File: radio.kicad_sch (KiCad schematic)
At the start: 27 parts, among them IC4 S2-LPQTR, IC5 BALF-SPI2-01D3, Y3 Crystal_GND24

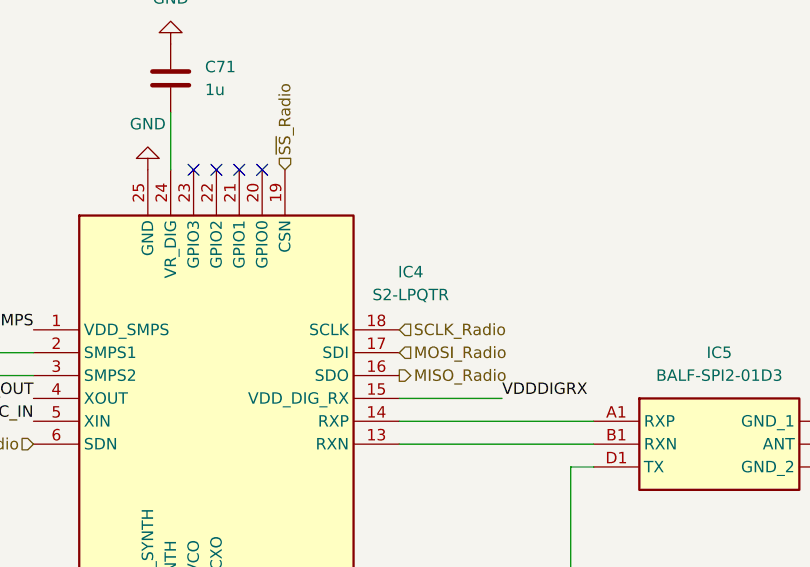
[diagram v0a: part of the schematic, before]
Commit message: Modify symbols of LDO and S2LP
Symbols for LDO and S2LP are inconsistent, because LDO VOUT pin was not in POWER OUTPUT type and S2LP wait for POWER INPUT on VDDS ... Moreover, decoupling capacitors on S2LP was a hell, because ERC break power flag transitivity on all passive components
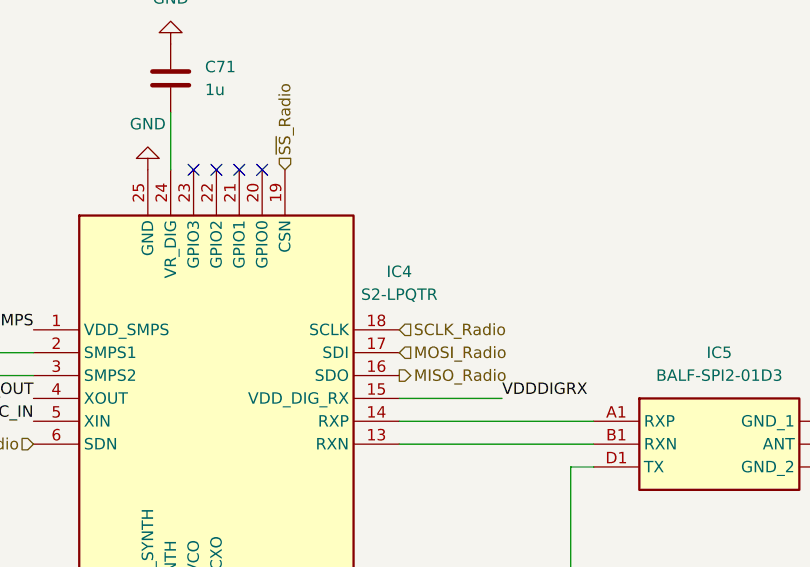
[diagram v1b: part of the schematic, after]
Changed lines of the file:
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@@
+	)
+	(symbol
+		(lib_id "weather-station-poc-sym:S2-LPQTR")
+		(at 127 74.93 0)
+		(unit 1)
+		(exclude_from_sim no)
+		(in_bom yes)
+		(on_board yes)
+		(dnp no)
+		(fields_autoplaced yes)
+		(property "Reference" "IC4"
+			(at 167.64 68.4745 0)
+			(effects
+				(font
+					(size 1.27 1.27)
+				)
+			)
+		)
+		(property "Value" "S2-LPQTR"
+			(at 167.64 71.0145 0)
+			(effects
+				(font
+					(size 1.27 1.27)
+				)
+			)
+		)
+		(property "Footprint" "weather-station-poc-fp:QFN50P400X400X100-25N-D"
+			(at 163.83 159.69 0)
+			(effects
+				(font
+					(size 1.27 1.27)
+				)
+				(justify left top)
+				(hide yes)
+			)
+		)
+		(property "Datasheet" "http://www.st.com/content/ccc/resource/technical/document/datasheet/group3/bd/26/62/81/3d/86/4d/15/DM00339133/files/DM00339133.pdf/jcr:content/translations/en.DM00339133.pdf"
+			(at 163.83 259.69 0)
+			(effects
+				(font
+					(size 1.27 1.27)
+				)
+				(justify left top)
+				(hide yes)
+			)
+		)
+		(property "Description" "STMICROELECTRONICS - S2-LPQTR - RF TRANSCEIVER, 1GHZ, QFN-24"
+			(at 127 74.93 0)
+			(effects
+				(font
+					(size 1.27 1.27)
+				)
+				(hide yes)
+			)
+		)
+		(property "Height" "1"
+			(at 163.83 459.69 0)
+			(effects
+				(font
+					(size 1.27 1.27)
+				)
+				(justify left top)
+				(hide yes)
+			)
+		)
+		(property "Mouser Part Number" "511-S2-LPQTR"
+			(at 163.83 559.69 0)
+			(effects
+				(font
+					(size 1.27 1.27)
+				)
+				(justify left top)
+				(hide yes)
+			)
+		)
+		(property "Mouser Price/Stock" "https://www.mouser.co.uk/ProductDetail/STMicroelectronics/S2-LPQTR?qs=pBOFM1sAujt3j15q4uNAuQ%3D%3D"
+			(at 163.83 659.69 0)
+			(effects
+				(font
+					(size 1.27 1.27)
+				)
+				(justify left top)
+				(hide yes)
+			)
+		)
+		(property "Manufacturer_Name" "STMicroelectronics"
+			(at 163.83 759.69 0)
+			(effects
+				(font
+					(size 1.27 1.27)
+				)
+				(justify left top)
+				(hide yes)
+			)
+		)
+		(property "Manufacturer_Part_Number" "S2-LPQTR"
+			(at 163.83 859.69 0)
+			(effects
+				(font
+					(size 1.27 1.27)
+				)
+				(justify left top)
+				(hide yes)
+			)
+		)
+		(pin "24"
+		)
+		(pin "12"
+		)
+		(pin "14"
+		)
+		(pin "20"
+		)
+		(pin "23"
+		)
+		(pin "8"
+		)
+		(pin "22"
+		)
+		(pin "17"
+		)
+		(pin "19"
+		)
+		(pin "6"
+		)
+		(pin "25"
+		)
+		(pin "21"
+		)
+		(pin "3"
+		)
+		(pin "10"
+		)
+		(pin "18"
+		)
+		(pin "2"
+		)
+		(pin "4"
+		)
+		(pin "9"
+		)
+		(pin "13"
+		)
+		(pin "11"
+		)
+		(pin "16"
+		)
+		(pin "1"
+		)
+		(pin "7"
+		)
+		(pin "15"
+		)
+		(pin "5"
+		)
+		(instances
+			(project ""
+				(path "/38eb53bb-294e-46e4-ad59-fd355ca373b9/31741ecc-719f-4191-b75e-d75152dfd251"
+					(reference "IC4")
+					(unit 1)
+				)
+			)
+		)
 	)
 	(symbol
@@
 					(unit 1)
 				)
-			)
-		)
-	)
-	(symbol
-		(lib_id "weather-station-poc-sym:S2-LPQTR")
-		(at 127 74.93 0)
-		(unit 1)
-		(exclude_from_sim no)
-		(in_bom yes)
-		(on_board yes)
-		(dnp no)
-		(fields_autoplaced yes)
-		(property "Reference" "IC4"
-			(at 168.91 68.5098 0)
-			(effects
-				(font
-					(size 1.27 1.27)
-				)
-			)
-		)
-		(property "Value" "S2-LPQTR"
-			(at 168.91 71.0498 0)
-			(effects
-				(font
-					(size 1.27 1.27)
-				)
-			)
-		)
-		(property "Footprint" "weather-station-poc-fp:QFN50P400X400X100-25N-D"
-			(at 163.83 159.69 0)
-			(effects
-				(font
-					(size 1.27 1.27)
-				)
-				(justify left top)
-				(hide yes)
-			)
-		)
-		(property "Datasheet" "http://www.st.com/content/ccc/resource/technical/document/datasheet/group3/bd/26/62/81/3d/86/4d/15/DM00339133/files/DM00339133.pdf/jcr:content/translations/en.DM00339133.pdf"
-			(at 163.83 259.69 0)
-			(effects
-				(font
-					(size 1.27 1.27)
-				)
-				(justify left top)
-				(hide yes)
-			)
-		)
-		(property "Description" "STMICROELECTRONICS - S2-LPQTR - RF TRANSCEIVER, 1GHZ, QFN-24"
-			(at 127 74.93 0)
-			(effects
-				(font
-					(size 1.27 1.27)
-				)
-				(hide yes)
-			)
-		)
-		(property "Height" "1"
-			(at 163.83 459.69 0)
-			(effects
-				(font
-					(size 1.27 1.27)
-				)
-				(justify left top)
-				(hide yes)
-			)
-		)
-		(property "Mouser Part Number" "511-S2-LPQTR"
-			(at 163.83 559.69 0)
-			(effects
-				(font
-					(size 1.27 1.27)
-				)
-				(justify left top)
-				(hide yes)
-			)
-		)
-		(property "Mouser Price/Stock" "https://www.mouser.co.uk/ProductDetail/STMicroelectronics/S2-LPQTR?qs=pBOFM1sAujt3j15q4uNAuQ%3D%3D"
-			(at 163.83 659.69 0)
-			(effects
-				(font
-					(size 1.27 1.27)
-				)
-				(justify left top)
-				(hide yes)
-			)
-		)
-		(property "Manufacturer_Name" "STMicroelectronics"
-			(at 163.83 759.69 0)
-			(effects
-				(font
-					(size 1.27 1.27)
-				)
-				(justify left top)
-				(hide yes)
-			)
-		)
-		(property "Manufacturer_Part_Number" "S2-LPQTR"
-			(at 163.83 859.69 0)
-			(effects
-				(font
-					(size 1.27 1.27)
-				)
-				(justify left top)
-				(hide yes)
-			)
-		)
-		(pin "17"
-		)
-		(pin "22"
-		)
-		(pin "12"
-		)
-		(pin "5"
-		)
-		(pin "25"
-		)
-		(pin "23"
-		)
-		(pin "11"
-		)
-		(pin "16"
-		)
-		(pin "3"
-		)
-		(pin "13"
-		)
-		(pin "9"
-		)
-		(pin "2"
-		)
-		(pin "20"
-		)
-		(pin "10"
-		)
-		(pin "8"
-		)
-		(pin "15"
-		)
-		(pin "7"
-		)
-		(pin "18"
-		)
-		(pin "14"
-		)
-		(pin "19"
-		)
-		(pin "24"
-		)
-		(pin "1"
-		)
-		(pin "4"
-		)
-		(pin "6"
-		)
-		(pin "21"
-		)
-		(instances
-			(project "weather-station-poc"
-				(path "/38eb53bb-294e-46e4-ad59-fd355ca373b9/31741ecc-719f-4191-b75e-d75152dfd251"
-					(reference "IC4")
-					(unit 1)
-				)

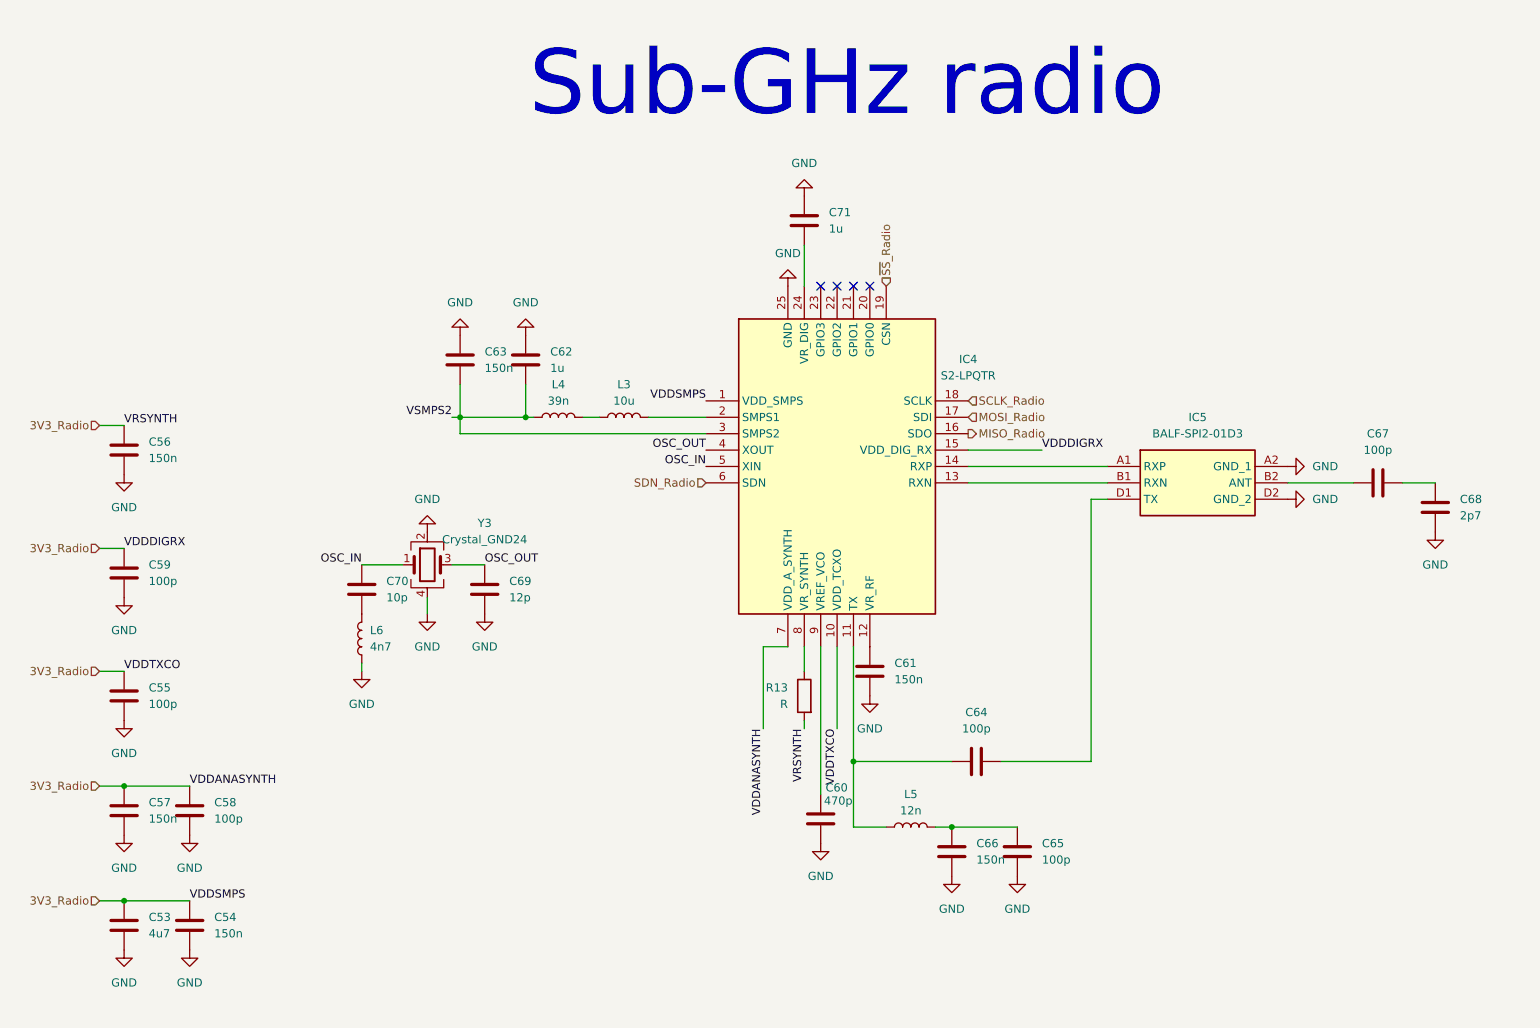
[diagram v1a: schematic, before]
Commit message: Functionnal block delimiting in schematics
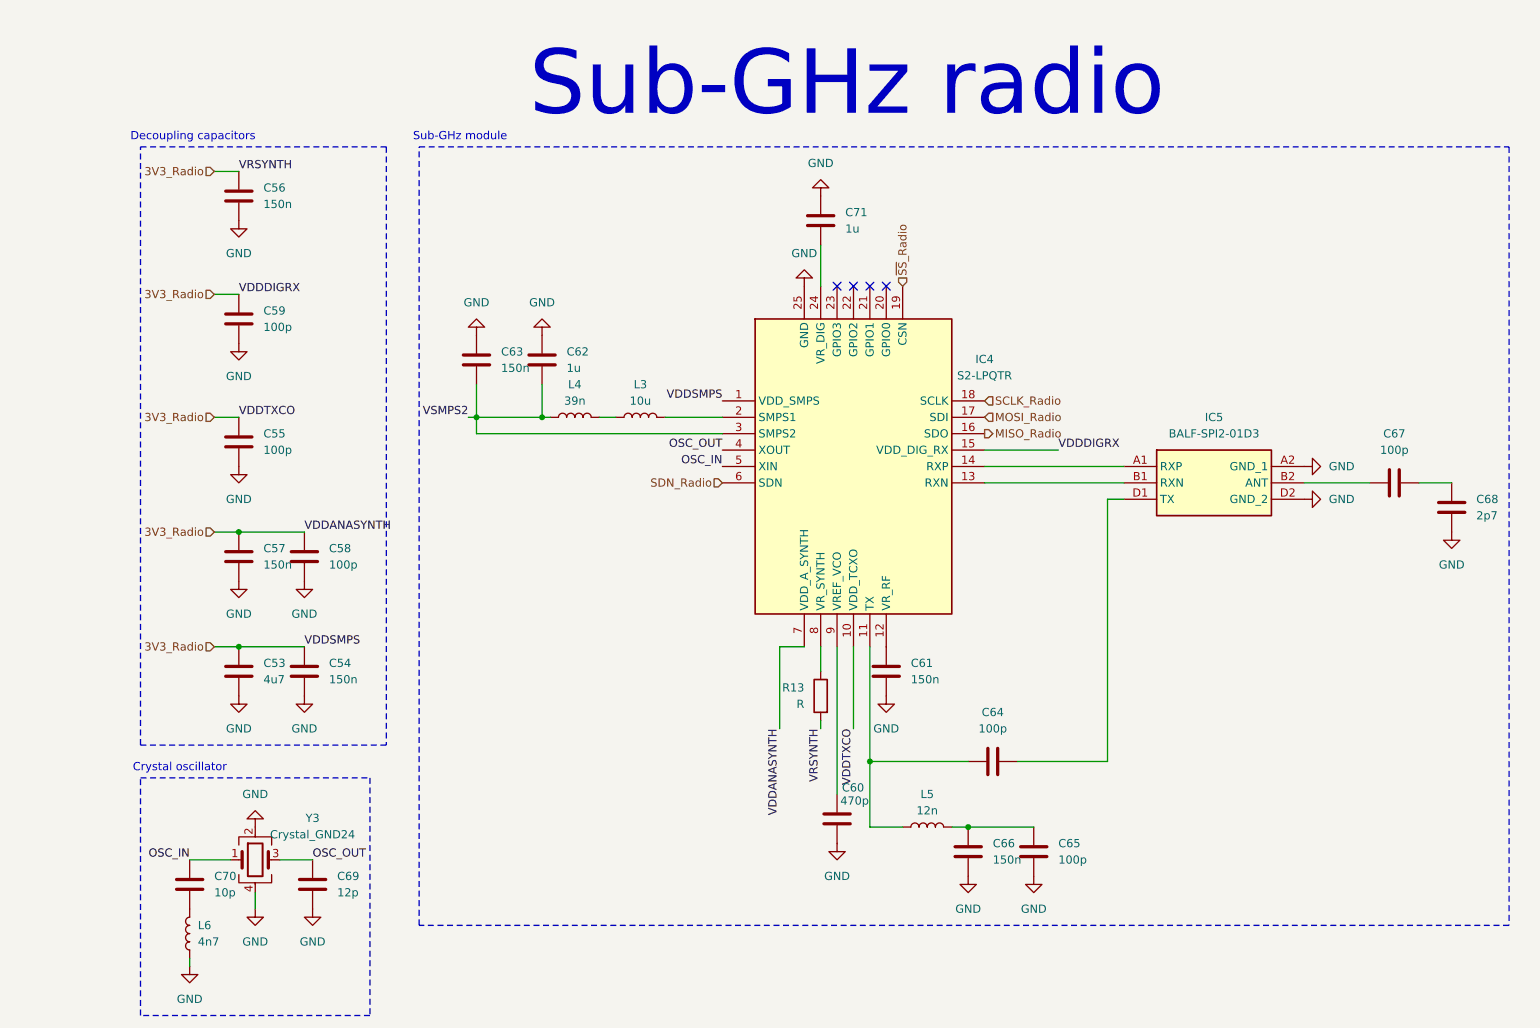
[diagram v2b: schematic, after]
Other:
- note added: "Crystal oscillator"
- note added: "Decoupling capacitors"
- note added: "Sub-GHz module"
- moved on the sheet: C53, C54, C55, C56, C57, C58, C59, C60, C61, C62, C63, C64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

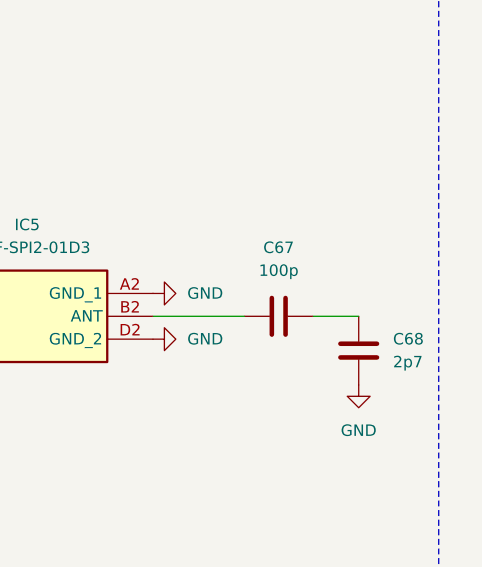
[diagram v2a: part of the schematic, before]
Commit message: Prepare Ethernet schematic (LAN8651)
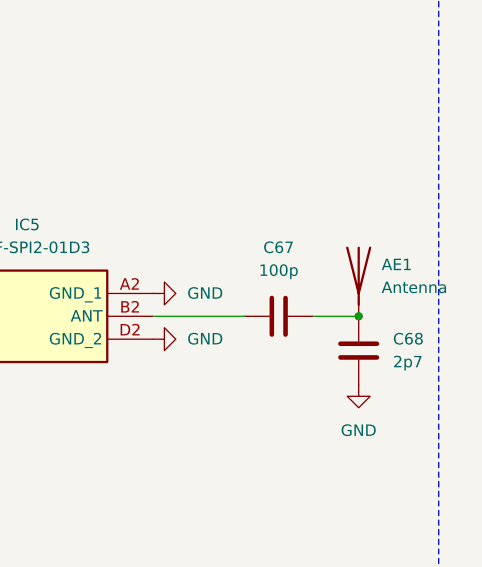
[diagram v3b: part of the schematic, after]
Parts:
- added AE1: Antenna, symbol Device:Antenna
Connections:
- net at C67.1, C68.2: now also AE1.1 (A)
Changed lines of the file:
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@@
 	)
 	(junction
+		(at 242.57 87.63)
+		(diameter 0)
+		(color 0 0 0 0)
+	)
+	(junction
 		(at 101.6 77.47)
 		(diameter 0)
@@
 					(unit 1)
 				)
+			)
+		)
+	)
+	(symbol
+		(lib_id "Device:Antenna")
+		(at 242.57 82.55 0)
+		(unit 1)
+		(exclude_from_sim no)
+		(in_bom yes)
+		(on_board yes)
+		(dnp no)
+		(fields_autoplaced yes)
+		(property "Reference" "AE1"
+			(at 245.11 81.9149 0)
+			(effects
+				(font
+					(size 1.27 1.27)
+				)
+				(justify left)
+			)
+		)
+		(property "Value" "Antenna"
+			(at 245.11 84.4549 0)
+			(effects
+				(font
+					(size 1.27 1.27)
+				)
+				(justify left)
+			)
+		)
+		(property "Footprint" ""
+			(at 242.57 82.55 0)
+			(effects
+				(font
+					(size 1.27 1.27)
+				)
+				(hide yes)
+			)
+		)
+		(property "Datasheet" "~"
+			(at 242.57 82.55 0)
+			(effects
+				(font
+					(size 1.27 1.27)
+				)
+				(hide yes)
+			)
+		)
+		(property "Description" "Antenna"
+			(at 242.57 82.55 0)
+			(effects
+				(font
+					(size 1.27 1.27)
+				)
+				(hide yes)
+			)
+		)
+		(pin "1"
+		)
+		(instances
+			(project ""
+				(path "/38eb53bb-294e-46e4-ad59-fd355ca373b9/31741ecc-719f-4191-b75e-d75152dfd251"
+					(reference "AE1")
+					(unit 1)
+				)

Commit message: Continue schematic review
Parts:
- removed C60: 470p, symbol Device:C
- added C96: 470p, symbol Device:C
- C71: value 1u -> 150n
- R13: value R -> 10
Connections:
- net 3V3_Radio: now also R13.1; no longer R13.2
- net GND: now also C61.2, C96.1; no longer C61.1
- net at IC4.12 (VR_RF): now also C61.1; no longer C61.2
- net at IC4.8 (VR_SYNTH): now also R13.2; no longer R13.1
- net at IC4.9 (VREF_VCO): now also C96.2
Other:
- moved on the sheet: C61, C64, C65, C66, L5
